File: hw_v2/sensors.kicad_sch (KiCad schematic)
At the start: 48 parts, among them U10 BMP280, U21 ADXL343, U23 MCP6004, U24 MCP6004, U6 TJA1051T-3

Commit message: WIP v7
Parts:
- removed C65, C67: 100nF, Capacitor_SMD:C_0402_1005Metric, symbol Device:C
- removed R103, R105: 6.8K, Resistor_SMD:R_0603_1608Metric, symbol Device:R
- removed R107, R109: 10K, Resistor_SMD:R_0603_1608Metric, symbol Device:R
- removed unit 1 of U24
- removed unit 3 of U24
- C50, R106: now in the parts list
- U4: now left out of the parts list
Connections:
- net at D16.1: no longer RN6.7 (R2.2)
- net CAM_MCU: no longer names the net of D16.4
- net CAM_MCU: no longer RN6.5 (R4.2)
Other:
- moved on the sheet: U24B, U24D

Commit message: hw v2
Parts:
- added TP10, TP11, TP14, TP15, TP16, TP17, TP18, TP9: TestPoint_Alt, TestPoint:TestPoint_Pad_1.0x1.0mm, symbol Connector:TestPoint_Alt
- U4: footprint OpenEFI_LIB:RusEFI_WBO -> hw_v2lib:WBO-module
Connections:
- net ACCL_CS: now also TP17.1
- net AT1_MCU: now also TP14.1
- net AT2_MCU: now also TP11.1
- net AT3_MCU: now also TP10.1
- net AT4_MCU: now also TP9.1
- net AV5_MCU: now also TP16.1
- net BARO_CS: now also TP18.1
- net Vbat_MCU: now also TP15.1

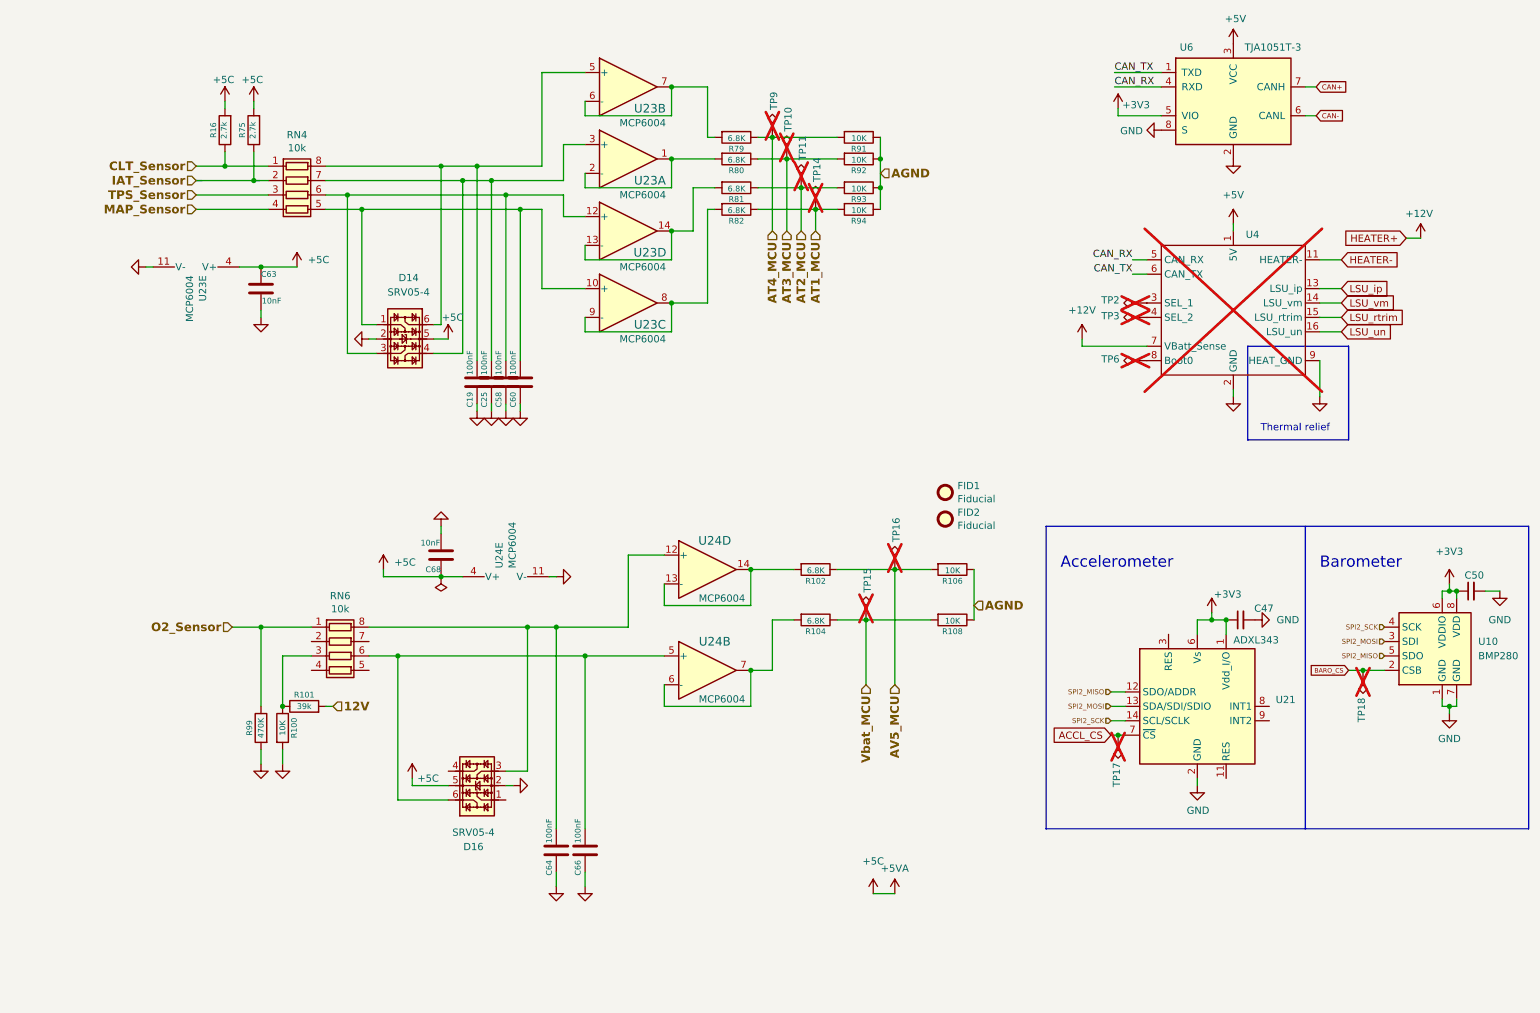
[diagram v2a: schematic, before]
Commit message: fix LCSC codes
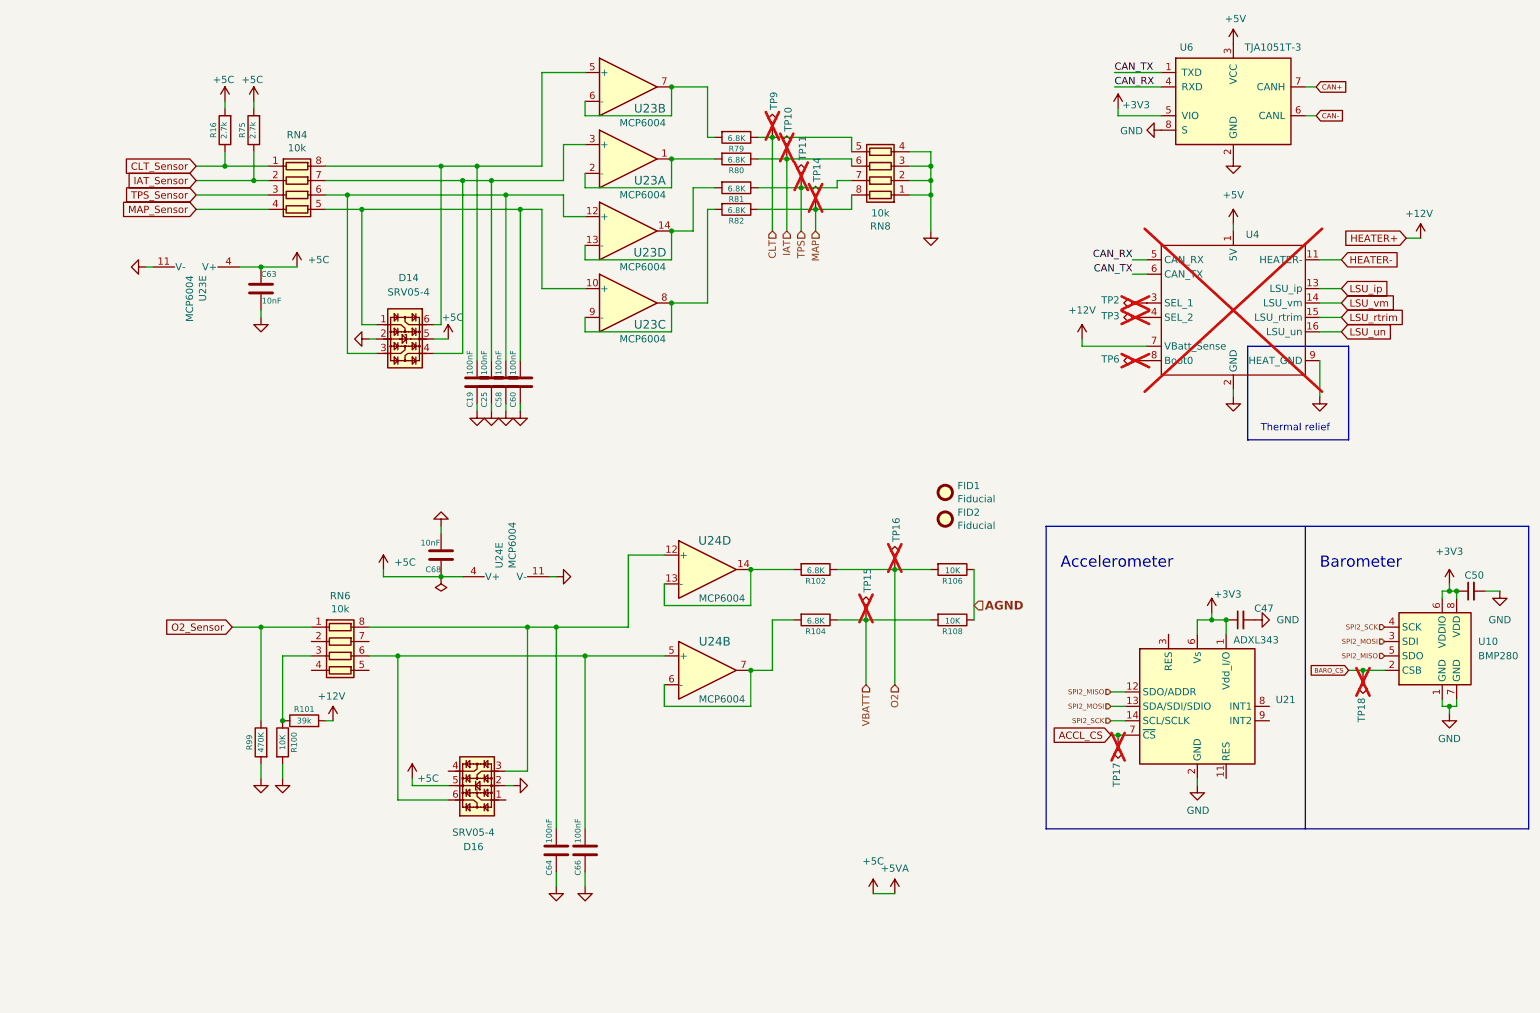
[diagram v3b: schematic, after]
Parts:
- removed R91, R92, R93, R94: 10K, Resistor_SMD:R_0603_1608Metric, symbol Device:R
- added RN8: 10k, Resistor_SMD:R_Array_Convex_4x0603, symbol Device:R_Pack04
- C64, C66, C68, D16, R100, R101, R102, R104, R108, RN6, U10, U21, U24: now in the parts list
- R99: footprint Resistor_SMD:R_0402_1005Metric -> Resistor_SMD:R_0603_1608Metric; now in the parts list
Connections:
- net 12V is gone; now on net +12V: R101.2
- net GND: now also RN8.1 (R1.1), RN8.2 (R2.1), RN8.3 (R3.1), RN8.4 (R4.1)
- net AT1_MCU renamed MAP
- net MAP: now also RN8.8 (R1.2)
- net AT2_MCU renamed TPS
- net TPS: now also RN8.7 (R2.2)
- net AT3_MCU renamed IAT
- net IAT: now also RN8.6 (R3.2)
- net AT4_MCU renamed CLT
- net CLT: now also RN8.5 (R4.2)
- net AV5_MCU renamed O2
- net Vbat_MCU renamed VBATT
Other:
- moved on the sheet: R100, R101, R99

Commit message: wip analog frontend & power
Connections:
- net CLT: now also RN8.4 (R4.1); no longer RN8.5 (R4.2)
- net CLT_Sensor: now also RN4.5 (R4.2); no longer RN4.1 (R1.1)
- net GND: now also RN8.5 (R4.2), RN8.6 (R3.2), RN8.7 (R2.2), RN8.8 (R1.2); no longer RN8.1 (R1.1), RN8.2 (R2.1), RN8.3 (R3.1), RN8.4 (R4.1)
- net IAT: now also RN8.3 (R3.1); no longer RN8.6 (R3.2)
- net IAT_Sensor: now also RN4.6 (R3.2); no longer RN4.2 (R2.1)
- net MAP: now also RN8.1 (R1.1); no longer RN8.8 (R1.2)
- net MAP_Sensor: now also RN4.8 (R1.2); no longer RN4.4 (R4.1)
- net TPS: now also RN8.2 (R2.1); no longer RN8.7 (R2.2)
- net TPS_Sensor: now also RN4.7 (R2.2); no longer RN4.3 (R3.1)
- net at C60.1, D14.1, U23.10 (+): now also RN4.1 (R1.1); no longer RN4.5 (R4.2)
- net at C58.1, D14.3, U23.12 (+): now also RN4.2 (R2.1); no longer RN4.6 (R3.2)
- net at C25.1, D14.4: now also RN4.3 (R3.1), U23.5 (+); no longer RN4.7 (R2.2), U23.3 (+)
- net at C19.1, D14.6: now also RN4.4 (R4.1), U23.3 (+); no longer RN4.8 (R1.2), U23.5 (+)
- net at U23.6 (-), U23.7: now also R80.2; no longer R79.2
- net at U23.1, U23.2 (-): now also R79.2; no longer R80.2
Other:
- moved on the sheet: RN4, RN8, U23A, U23B
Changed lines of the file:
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@@
 	)
 	(junction
-		(at 129.54 46.99)
+		(at 154.94 55.88)
 		(diameter 0)
 		(color 0 0 0 0)
 	)
 	(junction
-		(at 154.94 55.88)
+		(at 266.7 143.51)
 		(diameter 0)
 		(color 0 0 0 0)
 	)
 	(junction
-		(at 266.7 143.51)
+		(at 129.54 46.99)
 		(diameter 0)
 		(color 0 0 0 0)
@@
 	)
 	(junction
-		(at 129.54 34.29)
-		(diameter 0)
-		(color 0 0 0 0)
-	)
-	(junction
 		(at 57.15 66.04)
 		(diameter 0)
@@
 	)
 	(junction
+		(at 129.54 34.29)
+		(diameter 0)
+		(color 0 0 0 0)
+	)
+	(junction
 		(at 50.8 48.26)
 		(diameter 0)
@@
 	(symbol
 		(lib_id "Device:R_Pack04")
-		(at 63.5 53.34 270)
+		(at 63.5 50.8 90)
 		(unit 1)
 		(exclude_from_sim no)
@@
 		(dnp no)
 		(property "Reference" "RN4"
-			(at 63.5 42.7482 90)
+			(at 63.5 61.3918 90)
 			(effects
 				(font
@@
 		)
 		(property "Value" "10k"
-			(at 63.5 45.0596 90)
+			(at 63.5 59.0804 90)
 			(effects
 				(font
@@
 		)
 		(property "Footprint" "Resistor_SMD:R_Array_Convex_4x0603"
-			(at 63.5 60.325 90)
+			(at 63.5 43.815 90)
 			(effects
 				(font
@@
 		)
 		(property "Datasheet" "~"
-			(at 63.5 53.34 0)
+			(at 63.5 50.8 0)
 			(effects
 				(font
@@
 		)
 		(property "Description" ""
-			(at 63.5 53.34 0)
+			(at 63.5 50.8 0)
 			(effects
 				(font
@@
 		)
 		(property "Part #" "YC164-JR-0710KL"
-			(at 5.08 -40.64 0)
+			(at 121.92 144.78 0)
 			(effects
 				(font
@@
 		)
 		(property "VEND#" "YC164J-10KCT-ND"
-			(at 5.08 -40.64 0)
+			(at 121.92 144.78 0)
 			(effects
 				(font
@@
 		)
 		(property "VEND" "DIGI"
-			(at 5.08 -40.64 0)
+			(at 121.92 144.78 0)
 			(effects
 				(font
@@
 		)
 		(property "Manufacturer" "Yageo"
-			(at 5.08 -40.64 0)
+			(at 121.92 144.78 0)
 			(effects
 				(font
@@
 		)
 		(property "LCSC" "C29718"
-			(at 63.5 53.34 0)
+			(at 63.5 50.8 0)
 			(effects
 				(font
@@
 	(symbol
 		(lib_id "Amplifier_Operational:MCP6004")
-		(at 121.92 34.29 0)
+		(at 121.92 46.99 0)
 		(unit 2)
 		(exclude_from_sim no)
@@
 		(dnp no)
 		(property "Reference" "U23"
-			(at 125.73 38.1 0)
+			(at 125.73 50.8 0)
 			(effects
 				(font
@@
 		)
 		(property "Value" "MCP6004"
-			(at 124.46 40.64 0)
+			(at 124.46 53.34 0)
 			(effects
 				(font
@@
 		)
 		(property "Footprint" "Package_SO:TSSOP-14_4.4x5mm_P0.65mm"
-			(at 106.807 83.82 90)
+			(at 106.807 96.52 90)
 			(effects
 				(font
@@
 		)
 		(property "Datasheet" ""
-			(at 196.215 83.185 0)
+			(at 196.215 95.885 0)
 			(effects
 				(font
@@
 		)
 		(property "Description" ""
-			(at 121.92 34.29 0)
+			(at 121.92 46.99 0)
 			(effects
 				(font
@@
 		)
 		(property "Part #" "MCP6004T-I/ST"
-			(at -46.99 73.66 0)
+			(at -46.99 86.36 0)
 			(effects
 				(font
@@
 		)
 		(property "VEND#" "MCP6004T-I/STCT-ND"
-			(at -46.99 73.66 0)
+			(at -46.99 86.36 0)
 			(effects
 				(font
@@
 		)
 		(property "VEND" "DIGI"
-			(at -46.99 73.66 0)
+			(at -46.99 86.36 0)
 			(effects
 				(font
@@
 		)
 		(property "Manufacturer" "MicroChip"
-			(at -46.99 73.66 0)
+			(at -46.99 86.36 0)
 			(effects
 				(font
@@
 		)
 		(property "LCSC" "C248577"
-			(at 121.92 34.29 0)
+			(at 121.92 46.99 0)
 			(effects
 				(font
@@
 	(symbol
 		(lib_id "Amplifier_Operational:MCP6004")
-		(at 121.92 46.99 0)
+		(at 121.92 34.29 0)
 		(unit 1)
 		(exclude_from_sim no)
@@
 		(dnp no)
 		(property "Reference" "U23"
-			(at 125.73 50.8 0)
+			(at 124.968 37.846 0)
 			(effects
 				(font
@@
 		)
 		(property "Value" "MCP6004"
-			(at 124.46 53.34 0)
+			(at 124.46 40.64 0)
 			(effects
 				(font
@@
 		)
 		(property "Footprint" "Package_SO:TSSOP-14_4.4x5mm_P0.65mm"
-			(at 106.807 63.5 90)
+			(at 106.807 50.8 90)
 			(effects
 				(font
@@
 		)
 		(property "Datasheet" ""
-			(at 196.215 62.865 0)
+			(at 196.215 50.165 0)
 			(effects
 				(font
@@
 		)
 		(property "Description" ""
-			(at 121.92 46.99 0)
+			(at 121.92 34.29 0)
 			(effects
 				(font
@@
 		)
 		(property "Part #" "MCP6004T-I/ST"
-			(at -46.99 99.06 0)
+			(at -46.99 86.36 0)
 			(effects
 				(font
@@
 		)
 		(property "VEND#" "MCP6004T-I/STCT-ND"
-			(at -46.99 99.06 0)
+			(at -46.99 86.36 0)
 			(effects
 				(font
@@
 		)
 		(property "VEND" "DIGI"
-			(at -46.99 99.06 0)
+			(at -46.99 86.36 0)
 			(effects
 				(font
@@
 		)
 		(property "Manufacturer" "MicroChip"
-			(at -46.99 99.06 0)
+			(at -46.99 86.36 0)
 			(effects
 				(font
@@
 		)
 		(property "LCSC" "C248577"
-			(at 121.92 46.99 0)
+			(at 121.92 34.29 0)
 			(effects
 				(font
@@
 	(symbol
 		(lib_id "Device:R_Pack04")
-		(at 166.37 48.26 90)
+		(at 166.37 48.26 270)
+		(mirror x)
 		(unit 1)
 		(exclude_from_sim no)
@@
 		)
 		(property "Part #" "YC164-JR-0710KL"
-			(at 224.79 142.24 0)
+			(at 107.95 142.24 0)
 			(effects
 				(font
@@
 		)
 		(property "VEND#" "YC164J-10KCT-ND"
-			(at 224.79 142.24 0)
+			(at 107.95 142.24 0)
 			(effects
 				(font
@@
 		)
 		(property "VEND" "DIGI"
-			(at 224.79 142.24 0)
+			(at 107.95 142.24 0)
 			(effects
 				(font
@@
 		)
 		(property "Manufacturer" "Yageo"
-			(at 224.79 142.24 0)
+			(at 107.95 142.24 0)
 			(effects
 				(font

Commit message: wip analog frontend & power
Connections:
- net CLT: now also RN8.5 (R4.2); no longer RN8.4 (R4.1)
- net GND: now also RN8.1 (R1.1), RN8.2 (R2.1), RN8.3 (R3.1), RN8.4 (R4.1); no longer RN8.5 (R4.2), RN8.6 (R3.2), RN8.7 (R2.2), RN8.8 (R1.2)
- net IAT: now also RN8.6 (R3.2); no longer RN8.3 (R3.1)
- net MAP: now also RN8.8 (R1.2); no longer RN8.1 (R1.1)
- net TPS: now also RN8.7 (R2.2); no longer RN8.2 (R2.1)
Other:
- moved on the sheet: RN8
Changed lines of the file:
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@@
 	(symbol
 		(lib_id "Device:R_Pack04")
-		(at 166.37 48.26 270)
-		(mirror x)
+		(at 166.37 48.26 90)
 		(unit 1)
 		(exclude_from_sim no)
@@
 		)
 		(property "Part #" "YC164-JR-0710KL"
-			(at 107.95 142.24 0)
+			(at 224.79 142.24 0)
 			(effects
 				(font
@@
 		)
 		(property "VEND#" "YC164J-10KCT-ND"
-			(at 107.95 142.24 0)
+			(at 224.79 142.24 0)
 			(effects
 				(font
@@
 		)
 		(property "VEND" "DIGI"
-			(at 107.95 142.24 0)
+			(at 224.79 142.24 0)
 			(effects
 				(font
@@
 		)
 		(property "Manufacturer" "Yageo"
-			(at 107.95 142.24 0)
+			(at 224.79 142.24 0)
 			(effects
 				(font
